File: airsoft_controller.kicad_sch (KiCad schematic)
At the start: 65 parts, among them J1 Conn_01x03, J2 Conn_01x03, J3 Micro_SD_Card, J4 Conn_01x03, SW1 MEMBRANE, SW2 MEMBRANE, SW3 MECH_SW, SW4 MEMBRANE, SW5 MEMBRANE, SW6 MEMBRANE, SW7 MEMBRANE, U1 CP2102N-Axx-xQFN20, U2 ESP32-S3-WROOM-1, U3 74HC595, U4 SN74HCS165

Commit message: mounting holes, fixes silkscreen
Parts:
- renumbered R16 to R15, R17 to R16, R18 to R17, R19 to R18, R20 to R19, R21 to R20, R22 to R21
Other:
- added sheet Mount holes (mountholes.kicad_sch)

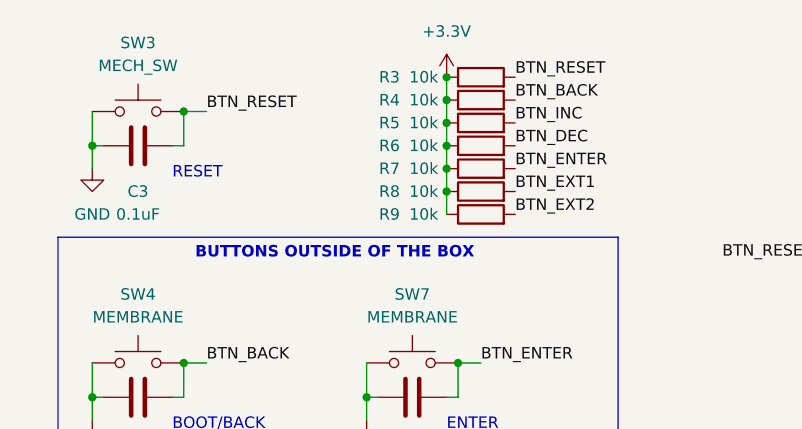
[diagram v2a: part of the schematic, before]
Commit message: minor setting changes in schematics, added test software container
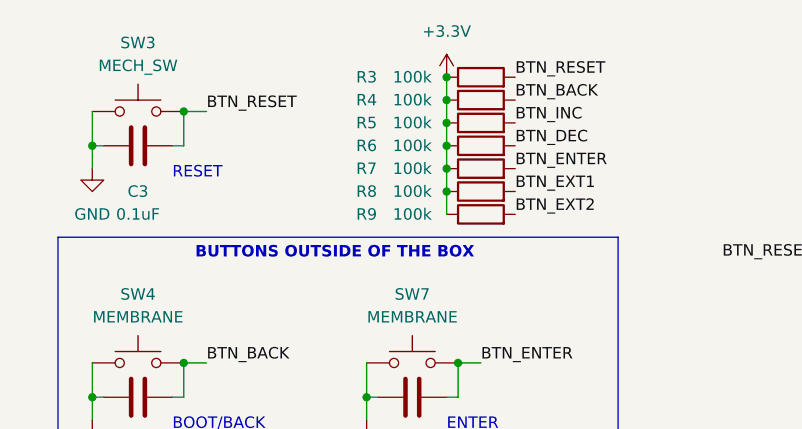
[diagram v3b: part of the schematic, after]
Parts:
- R3, R4, R5, R6, R7, R8, R9: value 10k -> 100k
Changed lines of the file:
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@@
   (symbol (lib_id "Device:R") (at 62.23 19.05 90) (unit 1)
     (in_bom yes) (on_board yes)
-    (property "Reference" "R3" (id 0) (at 52.07 19.05 90))
-    (property "Value" "10k" (id 1) (at 55.88 19.05 90))
+    (property "Reference" "R3" (id 0) (at 49.53 19.05 90))
+    (property "Value" "100k" (id 1) (at 54.61 19.05 90))
     (property "Footprint" "Resistor_SMD:R_0603_1608Metric_Pad0.98x0.95mm_HandSolder" (id 2) (at 62.23 20.828 90)
       (effects (font (size 1.27 1.27)) hide)
@@
   (symbol (lib_id "Device:R") (at 62.23 34.29 90) (unit 1)
     (in_bom yes) (on_board yes)
-    (property "Reference" "R9" (id 0) (at 52.07 34.29 90))
-    (property "Value" "10k" (id 1) (at 55.88 34.29 90))
+    (property "Reference" "R9" (id 0) (at 49.53 34.29 90))
+    (property "Value" "100k" (id 1) (at 54.61 34.29 90))
     (property "Footprint" "Resistor_SMD:R_0603_1608Metric_Pad0.98x0.95mm_HandSolder" (id 2) (at 62.23 36.068 90)
       (effects (font (size 1.27 1.27)) hide)
@@
   (symbol (lib_id "Device:R") (at 62.23 26.67 90) (unit 1)
     (in_bom yes) (on_board yes)
-    (property "Reference" "R6" (id 0) (at 52.07 26.67 90))
-    (property "Value" "10k" (id 1) (at 55.88 26.67 90))
+    (property "Reference" "R6" (id 0) (at 49.53 26.67 90))
+    (property "Value" "100k" (id 1) (at 54.61 26.67 90))
     (property "Footprint" "Resistor_SMD:R_0603_1608Metric_Pad0.98x0.95mm_HandSolder" (id 2) (at 62.23 28.448 90)
       (effects (font (size 1.27 1.27)) hide)
@@
   (symbol (lib_id "Device:R") (at 62.23 24.13 90) (unit 1)
     (in_bom yes) (on_board yes)
-    (property "Reference" "R5" (id 0) (at 52.07 24.13 90))
-    (property "Value" "10k" (id 1) (at 55.88 24.13 90))
+    (property "Reference" "R5" (id 0) (at 49.53 24.13 90))
+    (property "Value" "100k" (id 1) (at 54.61 24.13 90))
     (property "Footprint" "Resistor_SMD:R_0603_1608Metric_Pad0.98x0.95mm_HandSolder" (id 2) (at 62.23 25.908 90)
       (effects (font (size 1.27 1.27)) hide)
@@
   (symbol (lib_id "Device:R") (at 62.23 29.21 90) (unit 1)
     (in_bom yes) (on_board yes)
-    (property "Reference" "R7" (id 0) (at 52.07 29.21 90))
-    (property "Value" "10k" (id 1) (at 55.88 29.21 90))
+    (property "Reference" "R7" (id 0) (at 49.53 29.21 90))
+    (property "Value" "100k" (id 1) (at 54.61 29.21 90))
     (property "Footprint" "Resistor_SMD:R_0603_1608Metric_Pad0.98x0.95mm_HandSolder" (id 2) (at 62.23 30.988 90)
       (effects (font (size 1.27 1.27)) hide)
@@
   (symbol (lib_id "Device:R") (at 62.23 31.75 90) (unit 1)
     (in_bom yes) (on_board yes)
-    (property "Reference" "R8" (id 0) (at 52.07 31.75 90))
-    (property "Value" "10k" (id 1) (at 55.88 31.75 90))
+    (property "Reference" "R8" (id 0) (at 49.53 31.75 90))
+    (property "Value" "100k" (id 1) (at 54.61 31.75 90))
     (property "Footprint" "Resistor_SMD:R_0603_1608Metric_Pad0.98x0.95mm_HandSolder" (id 2) (at 62.23 33.528 90)
       (effects (font (size 1.27 1.27)) hide)
@@
   (symbol (lib_id "Device:R") (at 62.23 21.59 90) (unit 1)
     (in_bom yes) (on_board yes)
-    (property "Reference" "R4" (id 0) (at 52.07 21.59 90))
-    (property "Value" "10k" (id 1) (at 55.88 21.59 90))
+    (property "Reference" "R4" (id 0) (at 49.53 21.59 90))
+    (property "Value" "100k" (id 1) (at 54.61 21.59 90))
     (property "Footprint" "Resistor_SMD:R_0603_1608Metric_Pad0.98x0.95mm_HandSolder" (id 2) (at 62.23 23.368 90)
       (effects (font (size 1.27 1.27)) hide)
@@
     )
     (path "/153a78aa-a516-4463-8123-39c1ae70746f"
-      (reference "R3") (unit 1) (value "10k") (footprint "Resistor_SMD:R_0603_1608Metric_Pad0.98x0.95mm_HandSolder")
+      (reference "R3") (unit 1) (value "100k") (footprint "Resistor_SMD:R_0603_1608Metric_Pad0.98x0.95mm_HandSolder")
     )
     (path "/cef5b4bf-4e1f-4902-aa67-afa965075146"
-      (reference "R4") (unit 1) (value "10k") (footprint "Resistor_SMD:R_0603_1608Metric_Pad0.98x0.95mm_HandSolder")
+      (reference "R4") (unit 1) (value "100k") (footprint "Resistor_SMD:R_0603_1608Metric_Pad0.98x0.95mm_HandSolder")
     )
     (path "/8787105d-8ff9-48b0-bb1a-ade79ceb6ff8"
-      (reference "R5") (unit 1) (value "10k") (footprint "Resistor_SMD:R_0603_1608Metric_Pad0.98x0.95mm_HandSolder")
+      (reference "R5") (unit 1) (value "100k") (footprint "Resistor_SMD:R_0603_1608Metric_Pad0.98x0.95mm_HandSolder")
     )
     (path "/1e69beee-6a35-4a93-8130-29cbcdfaf495"
-      (reference "R6") (unit 1) (value "10k") (footprint "Resistor_SMD:R_0603_1608Metric_Pad0.98x0.95mm_HandSolder")
+      (reference "R6") (unit 1) (value "100k") (footprint "Resistor_SMD:R_0603_1608Metric_Pad0.98x0.95mm_HandSolder")
     )
     (path "/928969f0-c640-4531-a92f-d3ebb28badfa"
-      (reference "R7") (unit 1) (value "10k") (footprint "Resistor_SMD:R_0603_1608Metric_Pad0.98x0.95mm_HandSolder")
+      (reference "R7") (unit 1) (value "100k") (footprint "Resistor_SMD:R_0603_1608Metric_Pad0.98x0.95mm_HandSolder")
     )
     (path "/bbaa877e-d8b0-413f-aaa2-9ca45eeb5d88"
-      (reference "R8") (unit 1) (value "10k") (footprint "Resistor_SMD:R_0603_1608Metric_Pad0.98x0.95mm_HandSolder")
+      (reference "R8") (unit 1) (value "100k") (footprint "Resistor_SMD:R_0603_1608Metric_Pad0.98x0.95mm_HandSolder")
     )
     (path "/1a71d928-4a32-4bd7-97b1-2fcb5d2a4baa"
-      (reference "R9") (unit 1) (value "10k") (footprint "Resistor_SMD:R_0603_1608Metric_Pad0.98x0.95mm_HandSolder")
+      (reference "R9") (unit 1) (value "100k") (footprint "Resistor_SMD:R_0603_1608Metric_Pad0.98x0.95mm_HandSolder")
     )
     (path "/96d45ea0-9f44-468c-a355-40b7213be413"
@@
     )
     (path "/dad78a3c-8763-4d20-b96b-942d6d484c24/70712b41-0a4f-407d-b756-1dd7b8fa62c5/2bad7604-3810-4c09-9567-b30b41cedc7a"
-      (reference "R71") (unit 1) (value "60k") (footprint "Resistor_SMD:R_0603_1608Metric_Pad0.98x0.95mm_HandSolder")
+      (reference "R71") (unit 1) (value "62k") (footprint "Resistor_SMD:R_0603_1608Metric_Pad0.98x0.95mm_HandSolder")
     )
     (path "/dad78a3c-8763-4d20-b96b-942d6d484c24/70712b41-0a4f-407d-b756-1dd7b8fa62c5/3cf38dea-d081-471e-a3de-e3d804df952e"
@@
     )
     (path "/dad78a3c-8763-4d20-b96b-942d6d484c24/70712b41-0a4f-407d-b756-1dd7b8fa62c5/5fddb96c-282d-4675-ac2b-3fb1e4d0d036"
-      (reference "R73") (unit 1) (value "60k") (footprint "Resistor_SMD:R_0603_1608Metric_Pad0.98x0.95mm_HandSolder")
+      (reference "R73") (unit 1) (value "62k") (footprint "Resistor_SMD:R_0603_1608Metric_Pad0.98x0.95mm_HandSolder")
     )
     (path "/dad78a3c-8763-4d20-b96b-942d6d484c24/70712b41-0a4f-407d-b756-1dd7b8fa62c5/f2c34922-1c99-4d4c-b438-36c85403fe1d"
@@
     )
     (path "/dad78a3c-8763-4d20-b96b-942d6d484c24/70712b41-0a4f-407d-b756-1dd7b8fa62c5/fa0fb8f6-9369-44c9-9f9b-8d681e11815b"
-      (reference "R75") (unit 1) (value "60k") (footprint "Resistor_SMD:R_0603_1608Metric_Pad0.98x0.95mm_HandSolder")
+      (reference "R75") (unit 1) (value "62k") (footprint "Resistor_SMD:R_0603_1608Metric_Pad0.98x0.95mm_HandSolder")
     )
     (path "/dad78a3c-8763-4d20-b96b-942d6d484c24/70712b41-0a4f-407d-b756-1dd7b8fa62c5/0dc2ac1a-be4f-4ccd-8021-8b1556b811e7"
@@
     )
     (path "/dad78a3c-8763-4d20-b96b-942d6d484c24/70712b41-0a4f-407d-b756-1dd7b8fa62c5/4288761f-7fec-4f8c-8f7c-6fa929f793e8"
-      (reference "R77") (unit 1) (value "60k") (footprint "Resistor_SMD:R_0603_1608Metric_Pad0.98x0.95mm_HandSolder")
+      (reference "R77") (unit 1) (value "62k") (footprint "Resistor_SMD:R_0603_1608Metric_Pad0.98x0.95mm_HandSolder")
     )
     (path "/dad78a3c-8763-4d20-b96b-942d6d484c24/70712b41-0a4f-407d-b756-1dd7b8fa62c5/42cfab17-e414-4a96-b495-c915601418ea"
